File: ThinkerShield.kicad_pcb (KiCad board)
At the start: 2 copper layers, 69 x 69 mm, 38 parts, among them SW1 SW_PUSHBUTTON, SW2 SW_PUSHBUTTON, U1 BUZZER

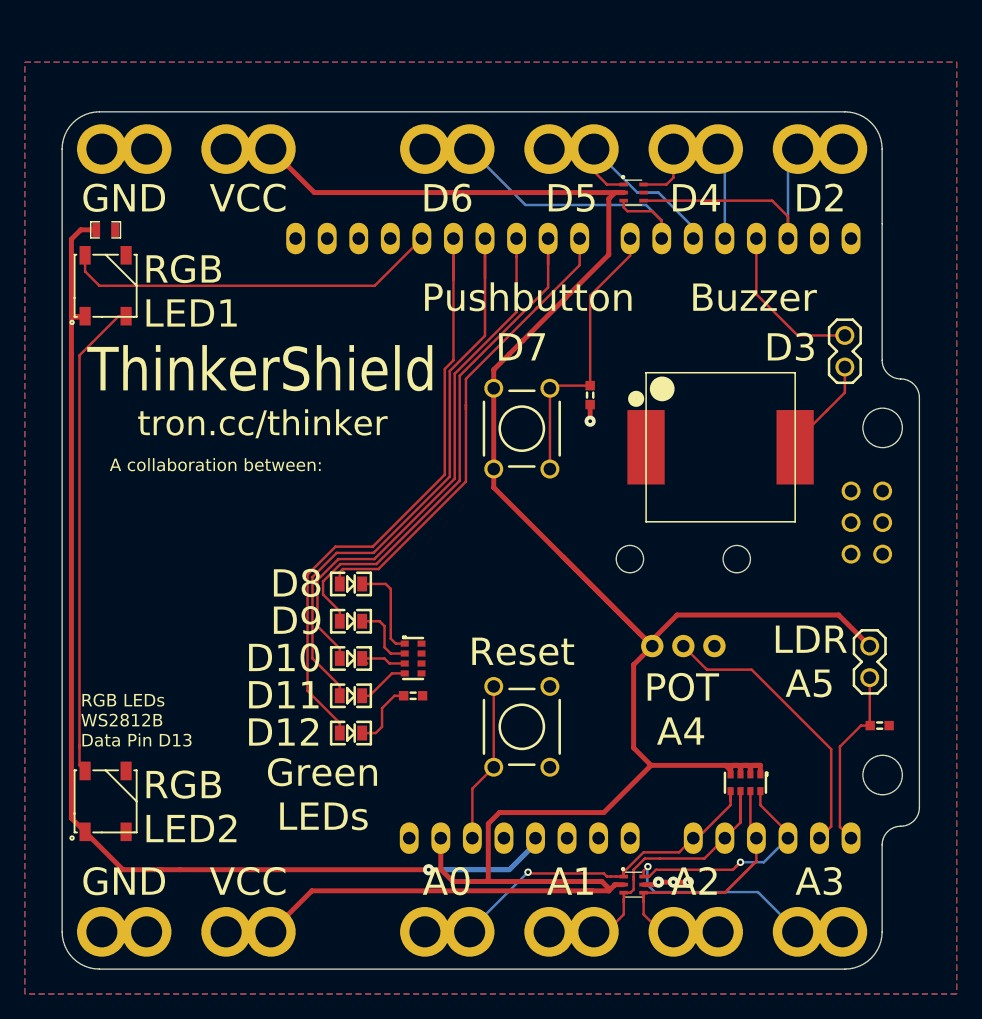
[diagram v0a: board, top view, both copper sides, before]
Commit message: Remove WS2812B LEDs, add sixth green LED for D13
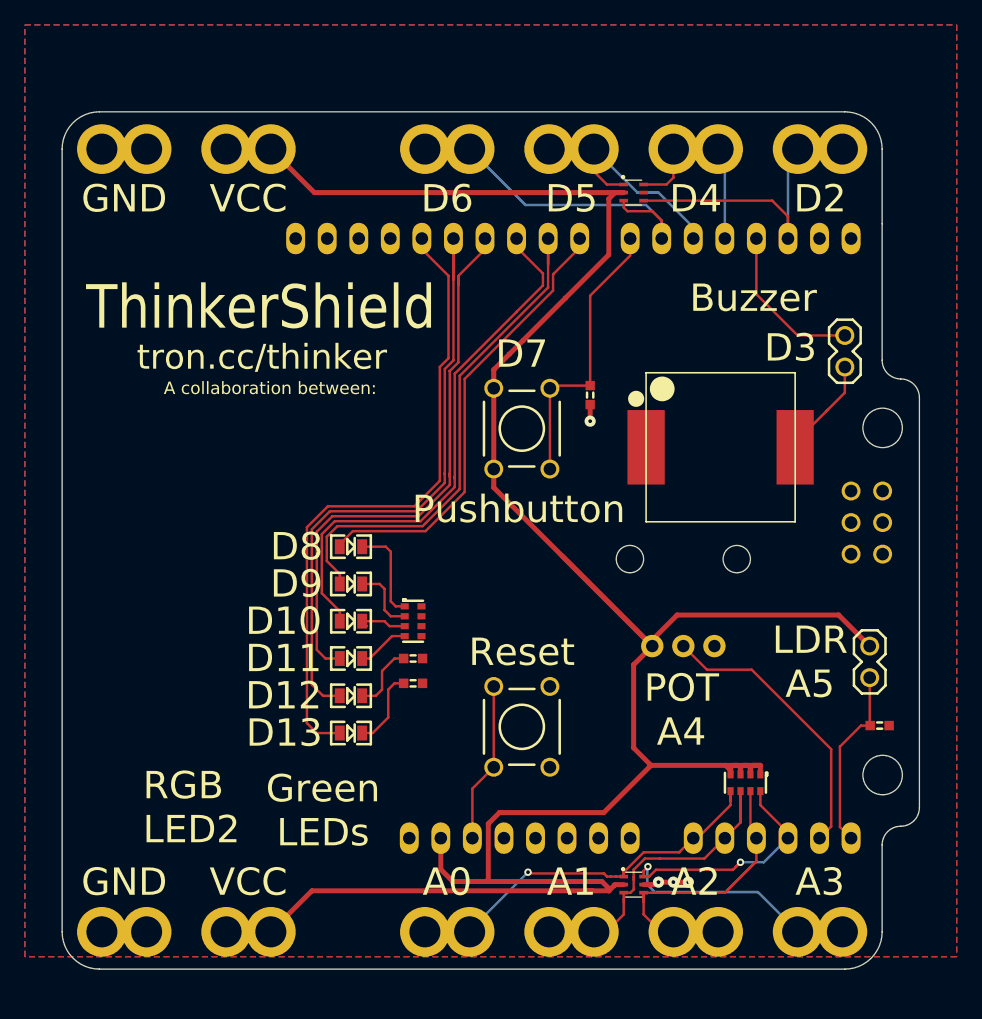
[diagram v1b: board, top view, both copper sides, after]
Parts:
- removed C1: 100nF, FT:0603_CAP
- removed LED7: WS2812B, FT:WS2812B
- added R6: 470R, FT:0603, F.Cu at (196.2, 90.0)
- LED6: value WS2812B -> GREEN; footprint FT:WS2812B -> FT:LED-0805
- moved LED6 41.1 mm to (191.2, 94.0), turned to 0 degrees
- moved LOGO_FREETRONICS 7.38 mm to (190.5, 69.5)
- moved G*** 6.70 mm to (178.5, 74.0)
- moved G*** 3.00 mm to (182.0, 67.0)
- moved LED1 3.00 mm to (191.2, 79.0)
- moved LED2 3.00 mm to (191.2, 82.0)
- moved LED3 3.00 mm to (191.2, 85.0)
- moved LED4 3.00 mm to (191.2, 88.0)
- moved LED5 3.00 mm to (191.2, 91.0)
- moved R3 3.00 mm to (196.2, 85.0)
- moved R4 3.00 mm to (196.2, 88.0)
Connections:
- SHIELD1 pad 5V: +5V -> (no net)
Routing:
- net +5V: track 91.5 -> 0.00 mm, vias 1 -> 0
- net Net-(LED6-Pad2): track 38.8 -> 0.00 mm
- net /D13: track 30.5 -> 51.7 mm
- net Net-(LED6-PadK): track 0.00 -> 6.31 mm
- net /D10: track 42.9 -> 44.6 mm
- net /D8: track 38.1 -> 37.0 mm
- net /D11: track 48.5 -> 47.5 mm
- net /D9: track 42.6 -> 41.7 mm
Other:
- board text added: "D13"
- board text removed: "RGB LED1"
- board text removed: "RGB LEDs WS2812B Data Pin D13"

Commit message: Rearrange ESD protection traces, update silkscreen
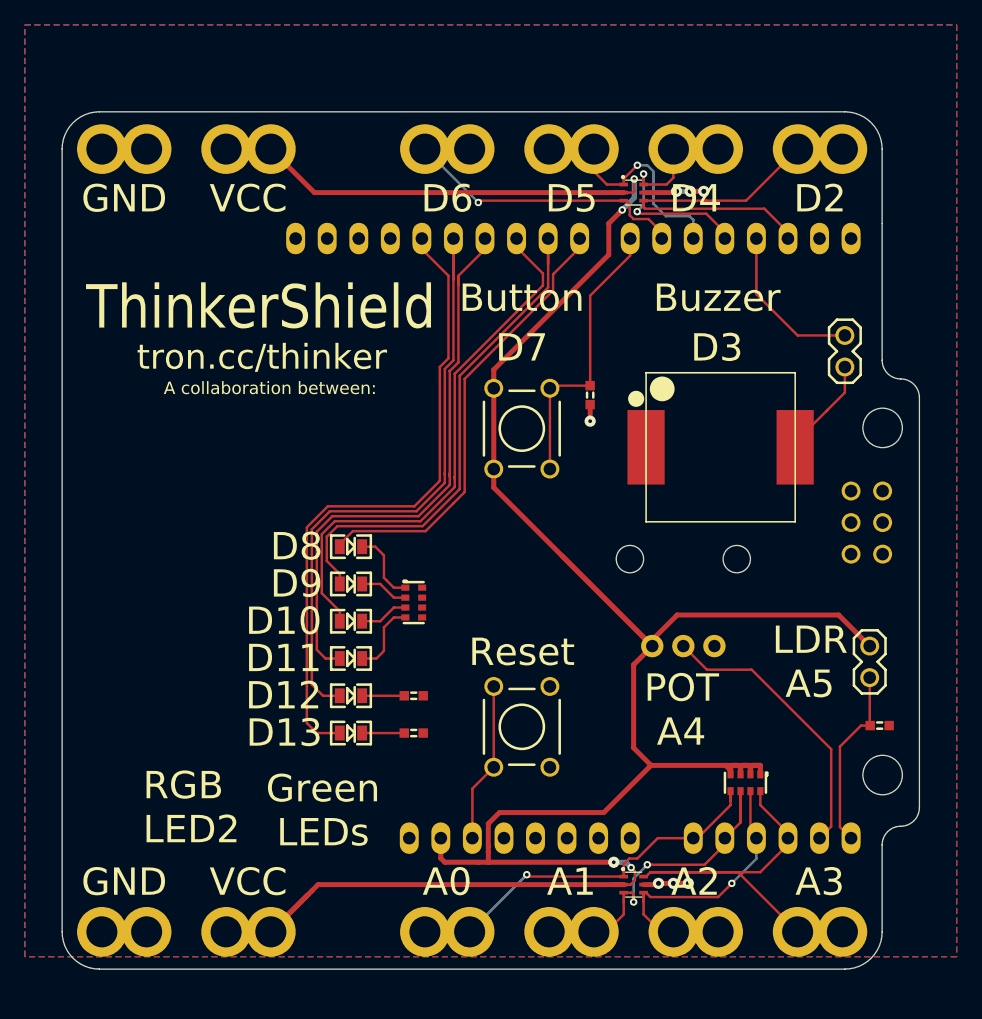
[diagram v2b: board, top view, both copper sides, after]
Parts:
- moved R6 4.00 mm to (196.3, 94.0)
- moved R4 3.00 mm to (196.3, 91.0)
- moved G*** 2.75 mm to (182.0, 69.8)
- moved R3 1.50 mm to (196.3, 83.5)
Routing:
- net IORef: track 207.6 -> 216.6 mm, vias 0 -> 4
- net /D2: track 25.0 -> 32.3 mm
- net /D4: track 16.0 -> 21.6 mm, vias 0 -> 2
- net GND: track 12.2 -> 17.5 mm, vias 4 -> 7
- net /A2: track 28.4 -> 25.2 mm, vias 0 -> 1
- net Net-(LED6-PadK): track 6.31 -> 3.39 mm
- net /A3: track 37.9 -> 35.3 mm, vias 2 -> 0
- net Net-(LED5-PadK): track 5.46 -> 3.39 mm
- net Net-(LED1-PadK): track 7.76 -> 5.90 mm
- net Net-(LED4-PadK): track 4.17 -> 5.96 mm
- net /D6: track 28.4 -> 26.8 mm, vias 0 -> 1
- net Net-(LED2-PadK): track 5.50 -> 3.93 mm
- net /A1: track 28.6 -> 30.0 mm, vias 0 -> 2
- net /D5: track 19.7 -> 20.5 mm, vias 0 -> 1
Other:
- board text added: "Button"
- board text added: "SKU: THINK Designed by Angus Gratton and MAAS"
- board text removed: "Pushbutton"
- board text removed: "SKU: THINK Designed by Angus Gratton"

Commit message: Swap TVDS to SMF05C, swap 22M resistors to individual, add body outline around RV09
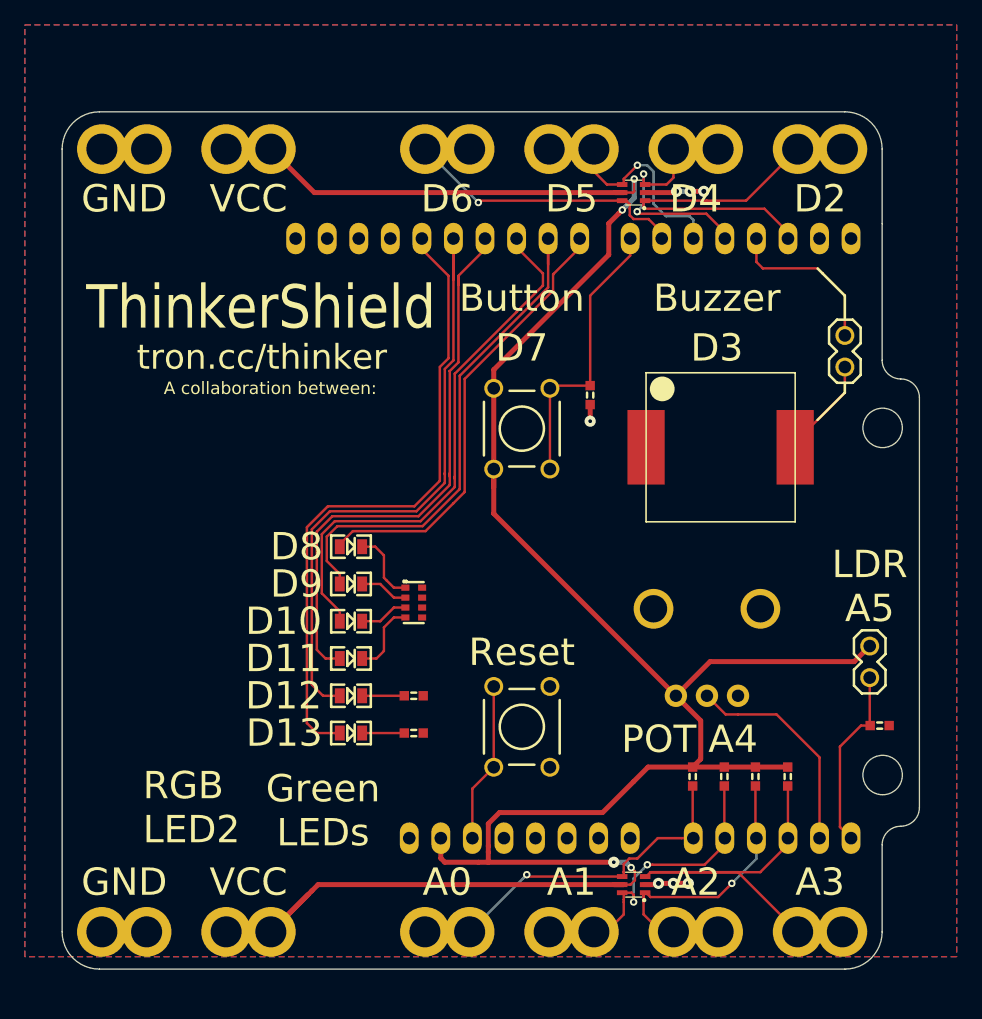
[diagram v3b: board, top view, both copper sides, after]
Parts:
- added R7: 22M, FT:0603, F.Cu at (221.3, 97.5)
- added R8: 22M, FT:0603, F.Cu at (223.8, 97.5)
- added R9: 22M, FT:0603, F.Cu at (226.4, 97.5)
- PH1: value 200K LDR -> LDR GL5516
- R1: value 10K -> 1K
- R5: footprint FT:RES_CAY16 -> FT:0603
- TV1: value ESD5V3U4RRS -> SMF05C
- TV2: value ESD5V3U4RRS -> SMF05C; footprint FT:SOT363 -> SOT363
- VR1: footprint FT:POT_RV09_VERT -> POT_RV09_VERT
- moved VR1 4.43 mm to (219.9, 84.0)
- moved R5 4.28 mm to (218.8, 97.5), turned to 90 degrees
- turned TV1 to 90 degrees
- turned TV2 to 90 degrees
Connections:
- R5 pad 1: IORef -> /A0
- R5 pad 2: /A3 -> IORef
- TV1 pad 1: /A0 -> /A2
- TV1 pad 2: IORef -> GND
- TV1 pad 3: /A1 -> /A3
- TV1 pad 4: /A2 -> /A0
- TV1 pad 5: GND -> IORef
- TV1 pad 6: /A3 -> /A1
- TV2 pad 1: /D5 -> /D2
- TV2 pad 2: IORef -> GND
- TV2 pad 3: /D6 -> /D4
- TV2 pad 4: /D2 -> /D5
- TV2 pad 5: GND -> IORef
- TV2 pad 6: /D4 -> /D6
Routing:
- net IORef: track 216.6 -> 201.3 mm
- net /A4: track 22.9 -> 17.6 mm
- net /A1: track 30.0 -> 27.4 mm
- net /A0: track 33.0 -> 31.5 mm
- net /A2: track 25.2 -> 26.2 mm

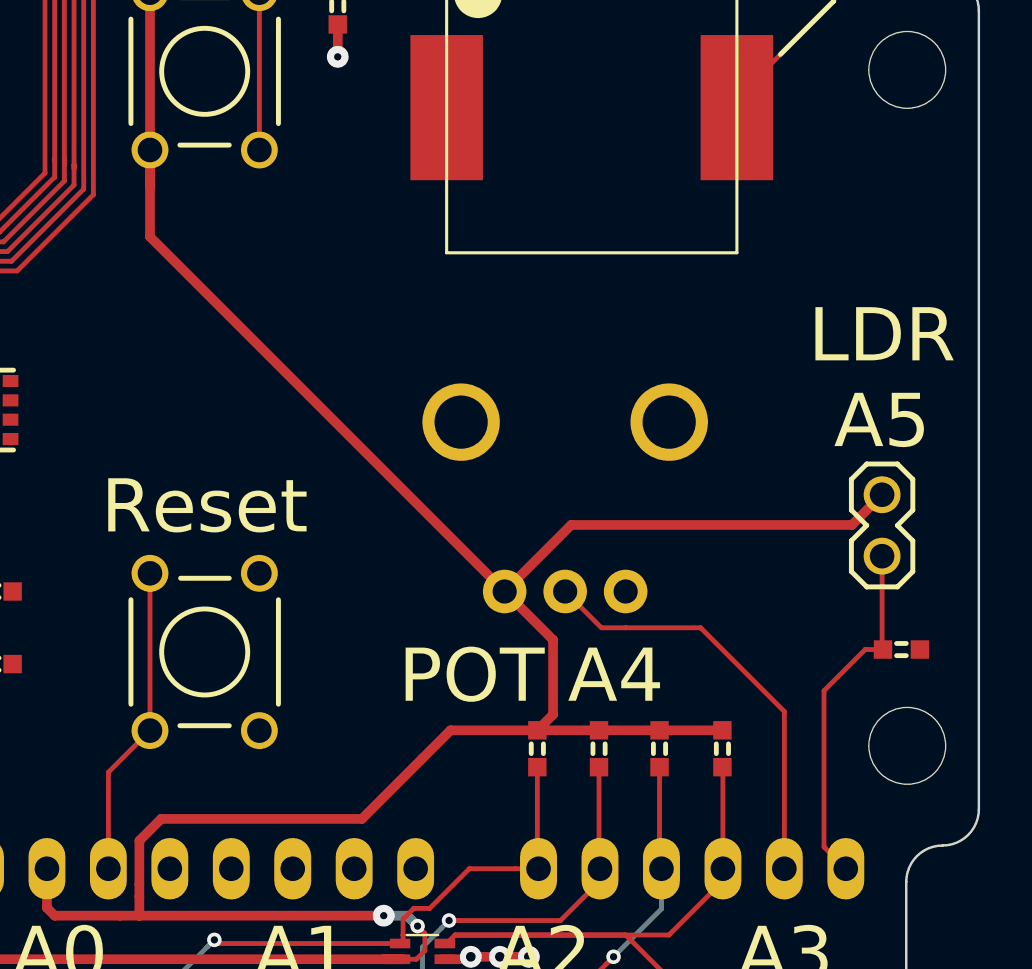
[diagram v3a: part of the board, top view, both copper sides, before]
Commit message: Swap pot orientation so CCW = min value
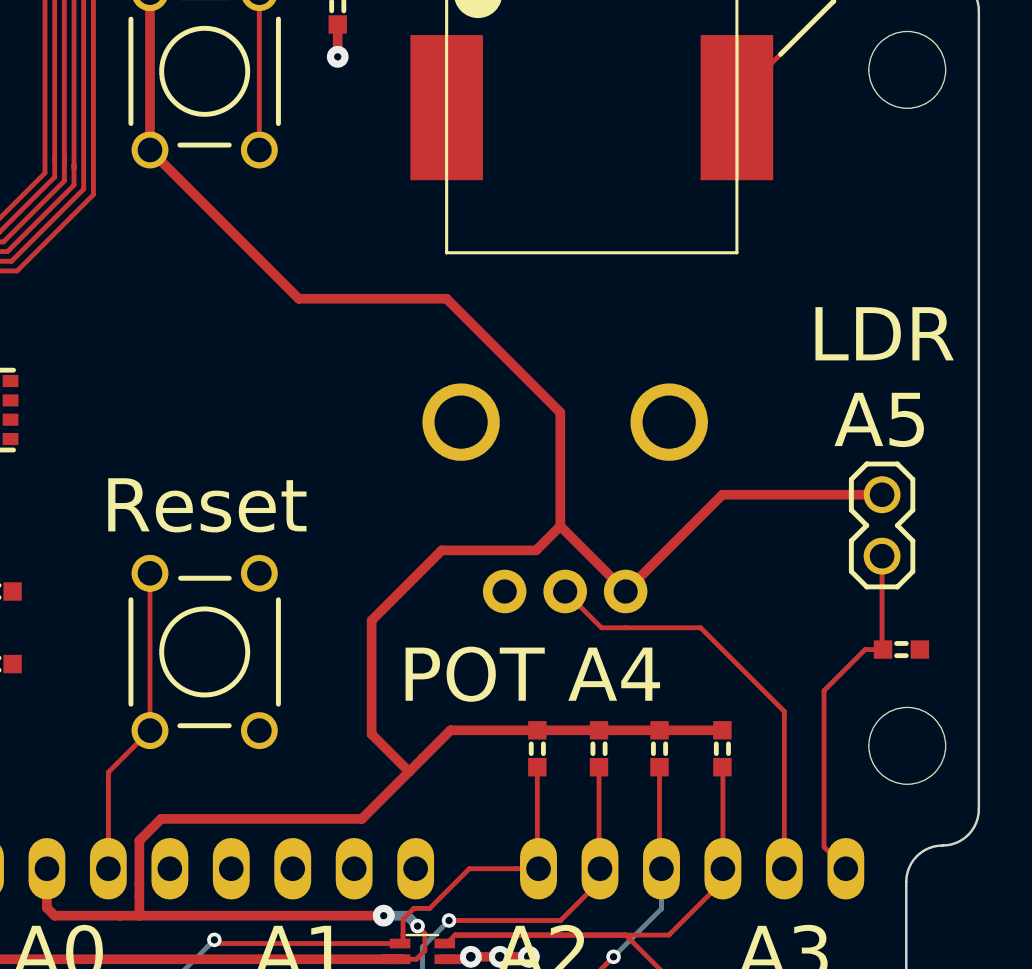
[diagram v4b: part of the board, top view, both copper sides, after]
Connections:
- VR1 pad 1: IORef -> GND
- VR1 pad 2: GND -> IORef
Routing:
- net IORef: track 201.3 -> 209.9 mm
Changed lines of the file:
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@@
     (links 84)
     (no_connects 0)
-    (area 165 37 240.000001 113.050001)
+    (area 167.949999 43.949999 237.050001 113.050001)
     (thickness 1.6)
     (drawings 54)
-    (tracks 334)
+    (tracks 338)
     (zones 0)
     (modules 40)
@@
       (net 24 /A4))
     (pad 1 thru_hole circle (at -2.5 7) (size 1.8 1.8) (drill 1) (layers *.Cu *.Mask F.SilkS)
+      (net 1 GND))
+    (pad 2 thru_hole circle (at 2.5 7) (size 1.8 1.8) (drill 1) (layers *.Cu *.Mask F.SilkS)
       (net 6 IORef))
-    (pad 2 thru_hole circle (at 2.5 7) (size 1.8 1.8) (drill 1) (layers *.Cu *.Mask F.SilkS)
-      (net 1 GND))
   )
   (module SOT363 (layer F.Cu)
@@
   (segment (start 215 105.55) (end 215.35 105.2) (width 0.2) (layer F.Cu) (net 5))
   (segment (start 214.8 105.55) (end 215 105.55) (width 0.2) (layer F.Cu) (net 5))
-  (segment (start 217.4 91) (end 219.4 93) (width 0.4) (layer F.Cu) (net 6))
-  (segment (start 219.4 96.088) (end 218.75 96.738) (width 0.4) (layer F.Cu) (net 6))
-  (segment (start 219.4 93) (end 219.4 96.088) (width 0.4) (layer F.Cu) (net 6))
-  (segment (start 217.4 91) (end 202.7394 76.3394) (width 0.4) (layer F.Cu) (net 6))
-  (segment (start 202.7394 76.3394) (end 202.7394 72.7512) (width 0.4) (layer F.Cu) (net 6))
-  (segment (start 217.4 91) (end 220.15 88.25) (width 0.4) (layer F.Cu) (net 6))
-  (segment (start 220.15 88.25) (end 231.75 88.25) (width 0.4) (layer F.Cu) (net 6))
-  (segment (start 202.7394 74.2394) (end 202.7394 72.7512) (width 0.4) (layer F.Cu) (net 6))
-  (segment (start 233 87) (end 231.75 88.25) (width 0.4) (layer F.Cu) (net 6))
+  (segment (start 219.7 88.3) (end 218.7 89.3) (width 0.4) (layer F.Cu) (net 6))
+  (segment (start 211.9 96.9) (end 213.45 98.45) (width 0.4) (layer F.Cu) (net 6))
+  (segment (start 211.9 92.2) (end 211.9 96.9) (width 0.4) (layer F.Cu) (net 6))
+  (segment (start 214.8 89.3) (end 211.9 92.2) (width 0.4) (layer F.Cu) (net 6))
+  (segment (start 218.7 89.3) (end 214.8 89.3) (width 0.4) (layer F.Cu) (net 6))
+  (segment (start 222.4 91) (end 219.7 88.3) (width 0.4) (layer F.Cu) (net 6))
+  (segment (start 208.8882 78.9) (end 202.7394 72.7512) (width 0.4) (layer F.Cu) (net 6))
+  (segment (start 215 78.9) (end 208.8882 78.9) (width 0.4) (layer F.Cu) (net 6))
+  (segment (start 219.7 83.6) (end 215 78.9) (width 0.4) (layer F.Cu) (net 6))
+  (segment (start 219.7 88.3) (end 219.7 83.6) (width 0.4) (layer F.Cu) (net 6))
+  (segment (start 233 87) (end 226.4 87) (width 0.4) (layer F.Cu) (net 6))
+  (segment (start 226.4 87) (end 222.4 91) (width 0.4) (layer F.Cu) (net 6))
   (segment (start 213.75 106.2) (end 214.099976 105.850024) (width 0.2) (layer F.Cu) (net 6))
   (segment (start 214.099976 105.850024) (end 214.099976 105.131344) (width 0.2) (layer F.Cu) (net 6))
@@
   (segment (start 213.368632 104.4) (end 213.499978 104.531346) (width 0.4) (layer B.Cu) (net 6))
   (segment (start 202.3 104.4) (end 202.3 103.6) (width 0.4) (layer F.Cu) (net 6))
-  (segment (start 214 97.9) (end 211.5 100.4) (width 0.4) (layer F.Cu) (net 6))
+  (segment (start 202.3 103.1) (end 202.3 103.6) (width 0.4) (layer F.Cu) (net 6))
+  (segment (start 202.3 101.3) (end 202.3 103.1) (width 0.4) (layer F.Cu) (net 6))
+  (segment (start 203.2 100.4) (end 202.3 101.3) (width 0.4) (layer F.Cu) (net 6))
+  (segment (start 211.5 100.4) (end 203.2 100.4) (width 0.4) (layer F.Cu) (net 6))
+  (segment (start 213.45 98.45) (end 211.5 100.4) (width 0.4) (layer F.Cu) (net 6))
+  (segment (start 214 97.9) (end 213.45 98.45) (width 0.4) (layer F.Cu) (net 6))
+  (segment (start 218.75 96.738) (end 215.162 96.738) (width 0.4) (layer F.Cu) (net 6))
   (segment (start 215.162 96.738) (end 214 97.9) (width 0.4) (layer F.Cu) (net 6))
-  (segment (start 218.75 96.738) (end 215.162 96.738) (width 0.4) (layer F.Cu) (net 6))
-  (segment (start 211.5 100.4) (end 203.2 100.4) (width 0.4) (layer F.Cu) (net 6))
-  (segment (start 203.2 100.4) (end 202.3 101.3) (width 0.4) (layer F.Cu) (net 6))
-  (segment (start 202.3 101.3) (end 202.3 103.1) (width 0.4) (layer F.Cu) (net 6))
-  (segment (start 202.3 103.1) (end 202.3 103.6) (width 0.4) (layer F.Cu) (net 6))
   (segment (start 212.4 104.4) (end 202.3 104.4) (width 0.4) (layer F.Cu) (net 6))
   (via (at 212.4 104.4) (size 0.9) (layers F.Cu B.Cu) (net 6))
